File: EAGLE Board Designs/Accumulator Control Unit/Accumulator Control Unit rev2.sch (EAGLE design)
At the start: 210 parts, among them J1 CONNECTOR-CAN_MF_T_V_, J2 CONNECTOR-8_MF_T_V_, J3 CONNECTOR-8_MF_T_V_, J4 CONNECTOR-2_MF_T_V_, J5 CONNECTOR-12_MF_T_V_, J6 CONNECTOR-14_MF_T_V_, Q1 TRANSISTOR_N_MOS__PMV15ENEA, Q2 TRANSISTOR_N_MOS__PMV15ENEA, Q3 TRANSISTOR_N_MOS__PMV15ENEA, Q4 TRANSISTOR_N_MOS__PMV15ENEA, T1 TRANSFORMER_HM2112ZNLT_AIRGAP, U1 RELAY_SOLIDSTATE_NO, U10 OPAMP_1_CHANNEL_OPA991, U11 LOGICGATE_AND_DCK3, U12 OPAMP_1_CHANNEL_OPA991, U13 OPAMP_1_CHANNEL_OPA991, U14 OPAMP_1_CHANNEL_OPA991, U15 LOGICGATE_AND_DCK3, U16 RELAY_SOLIDSTATE_NO, U17 VOLTAGE_REGULATOR_SOT223_3.3V, U18 OPAMP_1_CHANNEL_OPA991, U19 MAX7404, U2 ADG1423, U20 OPAMP_1_CHANNEL_OPA991, U21 LOGICGATE_BUFFER, U22 OPAMP_1_CHANNEL_OPA991, U25 TCAN1051HQV-Q1, U26 MAX7404, U27 OPAMP_1_CHANNEL_OPA991, U28 MAX7404, U29 OPAMP_1_CHANNEL_OPA991, U3 LM555, U30 MAX7404, U4 OPAMP_1_CHANNEL_OPA991, U5 LTC6820, U6 ADM8316WBX30, U7 OPAMP_1_CHANNEL_OPA991, U8 LOGICGATE_AND_DCK3, U9 OPAMP_1_CHANNEL_OPA991

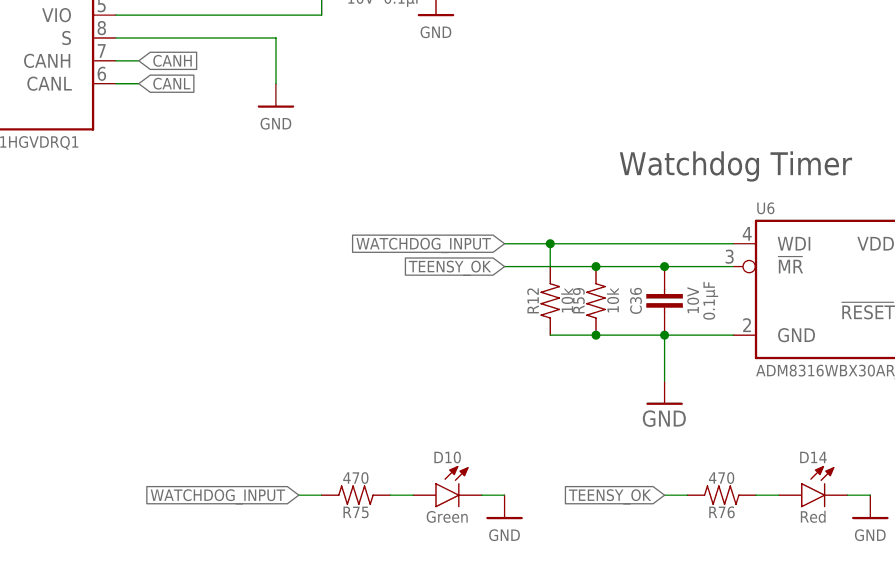
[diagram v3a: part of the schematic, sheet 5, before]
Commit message: all changes but board to board complete
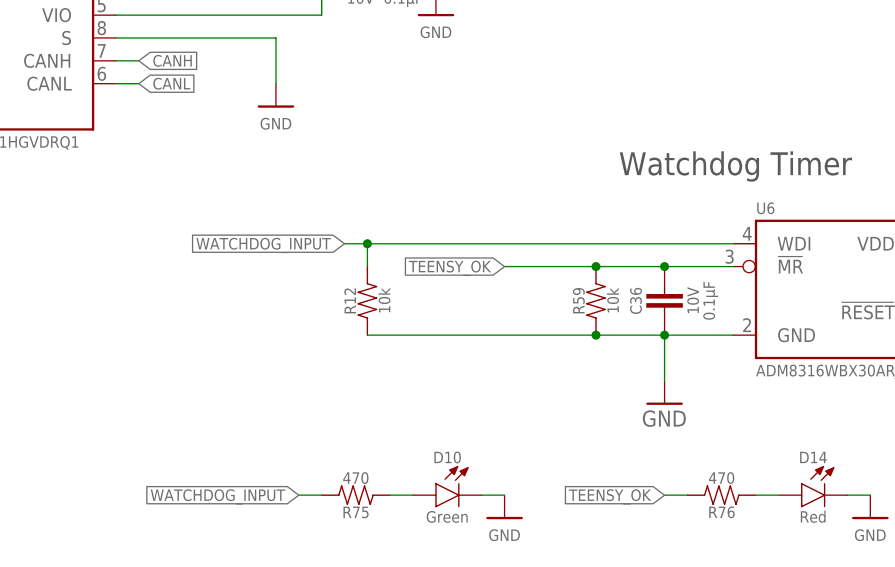
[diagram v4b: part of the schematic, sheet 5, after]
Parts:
- J1: value CONNECTOR-CAN_MF_T_V_ -> CONNECTOR-CAN_μF_S_RA_; device HyTechDevices - Copy:CONNECTOR-CAN_MF_T_V_ -> HyTechDevices:CONNECTOR-CAN_μF_S_RA_
- renumbered U$2 to U40
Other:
- moved on the sheet: R12
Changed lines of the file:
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@@
 <part name="D4" library="HyTechDevices - Copy" deviceset="TVS_*" device="" technology="8V"/>
 <part name="P5" library="HyTechSupplies" deviceset="GND" device=""/>
-<part name="J1" library="HyTechDevices - Copy" deviceset="CONNECTOR-CAN_?_*" device="MF_T_V"/>
+<part name="J1" library="HyTechDevices" deviceset="CONNECTOR-CAN_?_*" device="μF_S_RA"/>
 <part name="J5" library="HyTechDevices - Copy" deviceset="CONNECTOR-12_?_*" device="MF_T_V"/>
 <part name="J6" library="HyTechDevices - Copy" deviceset="CONNECTOR-14_?_*" device="MF_T_V"/>
@@
 <part name="R57" library="HyTechDevices" deviceset="RESISTOR_?_*" device="0603" technology="470"/>
 <part name="GND8" library="HyTechSupplies" deviceset="GND" device=""/>
-<part name="U$2" library="HyTechDevices" deviceset="RELAY_SOLIDSTATE_NO" device=""/>
+<part name="U40" library="HyTechDevices" deviceset="RELAY_SOLIDSTATE_NO" device=""/>
 <part name="R58" library="HyTechDevices - Copy" deviceset="RESISTOR_?_*" device="0603" technology="10K"/>
 <part name="R63" library="HyTechDevices - Copy" deviceset="RESISTOR_?_*" device="0603" technology="12K"/>
@@
 <attribute name="VALUE" x="228.6" y="168.91" size="1.27" layer="96" align="top-center"/>
 </instance>
-<instance part="P25" gate="1" x="38.1" y="99.06" smashed="yes">
-<attribute name="VALUE" x="38.1" y="97.79" size="1.27" layer="96" align="top-center"/>
+<instance part="P25" gate="1" x="38.1" y="101.6" smashed="yes">
+<attribute name="VALUE" x="38.1" y="100.33" size="1.27" layer="96" align="top-center"/>
 </instance>
 <instance part="U2" gate="S2" x="109.22" y="114.3" smashed="yes">
@@
 <pinref part="P25" gate="1" pin="GND"/>
 <wire x1="20.32" y1="104.14" x2="38.1" y2="104.14" width="0.1524" layer="91"/>
-<wire x1="38.1" y1="104.14" x2="38.1" y2="101.6" width="0.1524" layer="91"/>
 </segment>
 <segment>
@@
 </segment>
 <segment>
-<wire x1="22.86" y1="88.9" x2="25.4" y2="88.9" width="0.1524" layer="91"/>
+<pinref part="CURRENT_SENSE" gate="G$1" pin="P$1"/>
 <wire x1="22.86" y1="88.9" x2="25.4" y2="88.9" width="0.1524" layer="91"/>
 <label x="25.4" y="88.9" size="1.27" layer="95" xref="yes"/>
-<pinref part="CURRENT_SENSE" gate="G$1" pin="P$1"/>
 </segment>
 </net>
@@
 <attribute name="VALUE" x="203.2" y="115.57" size="1.27" layer="96" align="top-center"/>
 </instance>
-<instance part="U$2" gate="G$1" x="208.28" y="132.08" smashed="yes">
+<instance part="U40" gate="G$1" x="208.28" y="132.08" smashed="yes">
 <attribute name="NAME" x="208.28" y="132.842" size="1.27" layer="95"/>
 <attribute name="MPN" x="208.28" y="118.618" size="1.27" layer="96" align="top-left"/>
@@
 <wire x1="203.2" y1="121.92" x2="203.2" y2="119.38" width="0.1524" layer="91"/>
 <pinref part="GND8" gate="1" pin="GND"/>
-<pinref part="U$2" gate="G$1" pin="CONTROL-"/>
+<pinref part="U40" gate="G$1" pin="CONTROL-"/>
 </segment>
 <segment>
@@
 </segment>
 <segment>
-<pinref part="U$2" gate="G$1" pin="CONTACT2"/>
+<pinref part="U40" gate="G$1" pin="CONTACT2"/>
 <wire x1="228.6" y1="129.54" x2="231.14" y2="129.54" width="0.1524" layer="91"/>
 <wire x1="231.14" y1="129.54" x2="231.14" y2="134.62" width="0.1524" layer="91"/>
@@
 <wire x1="233.68" y1="116.84" x2="236.22" y2="116.84" width="0.1524" layer="91"/>
 <label x="236.22" y="116.84" size="1.27" layer="95" xref="yes"/>
-<pinref part="U$2" gate="G$1" pin="CONTACT1"/>
+<pinref part="U40" gate="G$1" pin="CONTACT1"/>
 <wire x1="228.6" y1="121.92" x2="233.68" y2="121.92" width="0.1524" layer="91"/>
 <junction x="233.68" y="121.92"/>
@@
 <pinref part="R57" gate="G$1" pin="2"/>
 <wire x1="200.66" y1="129.54" x2="205.74" y2="129.54" width="0.1524" layer="91"/>
-<pinref part="U$2" gate="G$1" pin="CONTROL+"/>
+<pinref part="U40" gate="G$1" pin="CONTROL+"/>
 </segment>
 </net>
@@
 <attribute name="VALUE" x="243.84" y="113.03" size="1.27" layer="96" align="bottom-center"/>
 </instance>
-<instance part="R12" gate="G$1" x="195.58" y="88.9" smashed="yes" rot="R90">
-<attribute name="NAME" x="194.31" y="87.63" size="1.27" layer="95" rot="R90" align="bottom-center"/>
-<attribute name="RESISTANCE" x="196.85" y="87.63" size="1.27" layer="96" rot="R90" align="top-center"/>
+<instance part="R12" gate="G$1" x="175.26" y="88.9" smashed="yes" rot="R90">
+<attribute name="NAME" x="173.99" y="87.63" size="1.27" layer="95" rot="R90" align="bottom-center"/>
+<attribute name="RESISTANCE" x="176.53" y="87.63" size="1.27" layer="96" rot="R90" align="top-center"/>
 </instance>
 <instance part="GND38" gate="1" x="208.28" y="76.2" smashed="yes">
@@
 <segment>
 <pinref part="R12" gate="G$1" pin="1"/>
-<wire x1="195.58" y1="83.82" x2="200.66" y2="83.82" width="0.1524" layer="91"/>
+<wire x1="175.26" y1="83.82" x2="200.66" y2="83.82" width="0.1524" layer="91"/>
 <pinref part="R59" gate="G$1" pin="1"/>
 <wire x1="200.66" y1="83.82" x2="208.28" y2="83.82" width="0.1524" layer="91"/>
@@
 <segment>
 <pinref part="R12" gate="G$1" pin="2"/>
-<wire x1="195.58" y1="93.98" x2="215.9" y2="93.98" width="0.1524" layer="91"/>
-<wire x1="195.58" y1="93.98" x2="195.58" y2="91.44" width="0.1524" layer="91"/>
-<label x="190.5" y="93.98" size="1.27" layer="95" rot="R180" xref="yes"/>
-<wire x1="195.58" y1="93.98" x2="190.5" y2="93.98" width="0.1524" layer="91"/>
-<junction x="195.58" y="93.98"/>
+<wire x1="175.26" y1="93.98" x2="215.9" y2="93.98" width="0.1524" layer="91"/>
+<wire x1="175.26" y1="93.98" x2="175.26" y2="91.44" width="0.1524" layer="91"/>
+<label x="172.72" y="93.98" size="1.27" layer="95" rot="R180" xref="yes"/>
+<wire x1="175.26" y1="93.98" x2="172.72" y2="93.98" width="0.1524" layer="91"/>
+<junction x="175.26" y="93.98"/>
 <pinref part="U6" gate="G$1" pin="WDI"/>
 </segment>

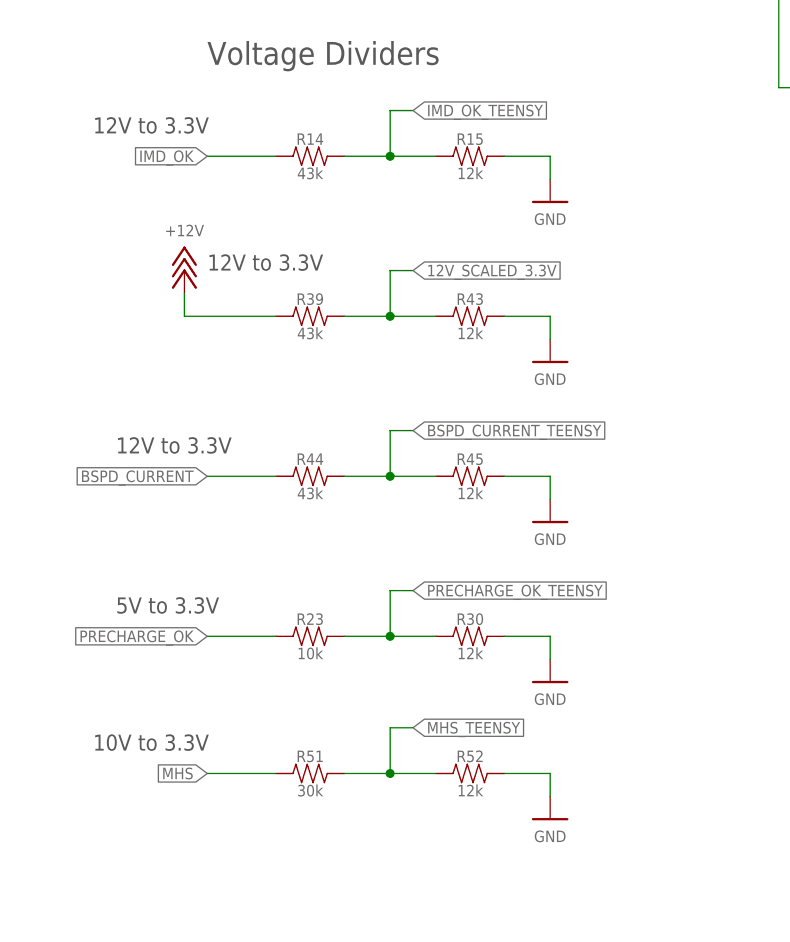
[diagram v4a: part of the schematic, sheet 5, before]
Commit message: changed voltage dividers
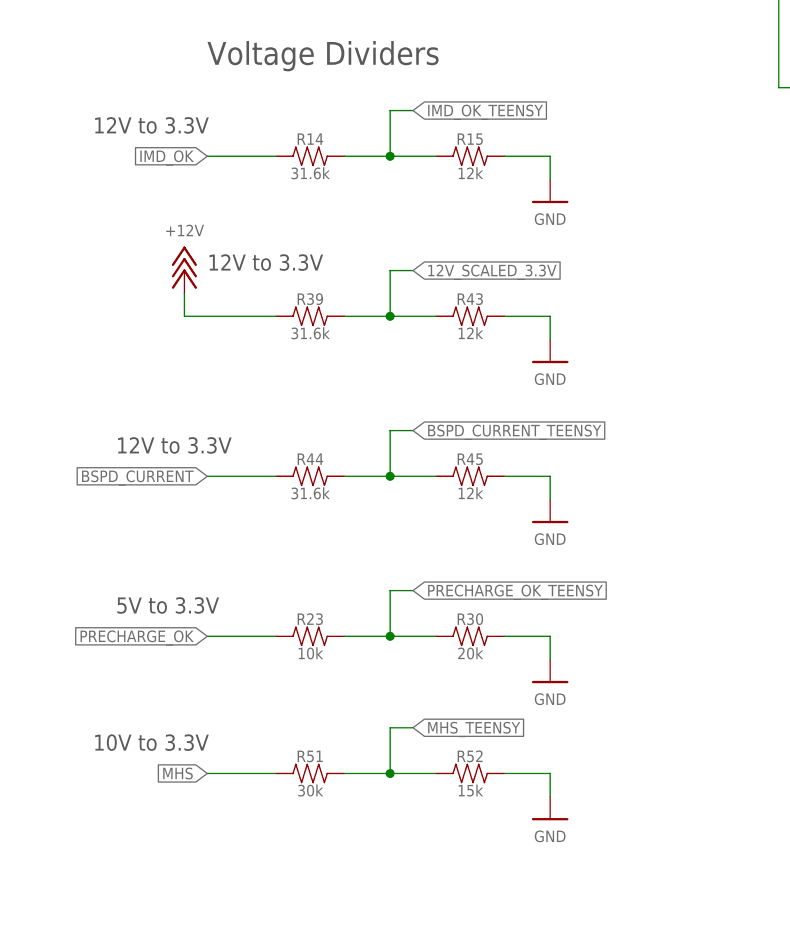
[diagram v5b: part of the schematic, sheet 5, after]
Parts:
- R14, R39, R44: value RESISTOR_0603_43K -> RESISTOR_0603_31.6K; device HyTechDevices - Copy:RESISTOR_0603_43K -> HyTechDevices:RESISTOR_0603_31.6K
- R30: value RESISTOR_0603_12K -> RESISTOR_0603_20K; device HyTechDevices - Copy:RESISTOR_0603_12K -> HyTechDevices:RESISTOR_0603_20K
- R52: value RESISTOR_0603_12K -> RESISTOR_0603_15K; device HyTechDevices - Copy:RESISTOR_0603_12K -> HyTechDevices:RESISTOR_0603_15K
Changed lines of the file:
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@@
 <part name="P58" library="HyTechSupplies" deviceset="GND" device=""/>
 <part name="P59" library="HyTechSupplies" deviceset="GND" device=""/>
-<part name="R14" library="HyTechDevices - Copy" deviceset="RESISTOR_?_*" device="0603" technology="43K"/>
+<part name="R14" library="HyTechDevices" deviceset="RESISTOR_?_*" device="0603" technology="31.6K" value="RESISTOR_0603_31.6K"/>
 <part name="R15" library="HyTechDevices - Copy" deviceset="RESISTOR_?_*" device="0603" technology="12K"/>
 <part name="P66" library="HyTechSupplies" deviceset="GND" device=""/>
 <part name="P67" library="HyTechSupplies" deviceset="GND" device=""/>
-<part name="R39" library="HyTechDevices - Copy" deviceset="RESISTOR_?_*" device="0603" technology="43K"/>
+<part name="R39" library="HyTechDevices" deviceset="RESISTOR_?_*" device="0603" technology="31.6K" value="RESISTOR_0603_31.6K"/>
 <part name="P68" library="HyTechSupplies" deviceset="GND" device=""/>
-<part name="R44" library="HyTechDevices - Copy" deviceset="RESISTOR_?_*" device="0603" technology="43K"/>
+<part name="R44" library="HyTechDevices" deviceset="RESISTOR_?_*" device="0603" technology="31.6K" value="RESISTOR_0603_31.6K"/>
 <part name="P69" library="HyTechSupplies" deviceset="GND" device=""/>
 <part name="P70" library="HyTechSupplies" deviceset="+12V" device=""/>
-<part name="R30" library="HyTechDevices - Copy" deviceset="RESISTOR_?_*" device="0603" technology="12K"/>
+<part name="R30" library="HyTechDevices" deviceset="RESISTOR_?_*" device="0603" technology="20K" value="RESISTOR_0603_20K"/>
 <part name="R23" library="HyTechDevices - Copy" deviceset="RESISTOR_?_*" device="0603" technology="10K"/>
 <part name="P72" library="HyTechSupplies" deviceset="+3V3" device=""/>
@@
 <part name="P82" library="HyTechSupplies" deviceset="GND" device=""/>
 <part name="C43" library="HyTechDevices - Copy" deviceset="CAPACITOR_?_*" device="0603" technology="10V_680PF"/>
-<part name="R52" library="HyTechDevices - Copy" deviceset="RESISTOR_?_*" device="0603" technology="12K"/>
+<part name="R52" library="HyTechDevices" deviceset="RESISTOR_?_*" device="0603" technology="15K" value="RESISTOR_0603_15K"/>
 <part name="P87" library="HyTechSupplies" deviceset="GND" device=""/>
 <part name="R51" library="HyTechDevices - Copy" deviceset="RESISTOR_?_*" device="0603" technology="30K"/>

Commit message: more changes
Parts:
- J3: value CONNECTOR-8_MF_T_V_ -> CONNECTOR-8_FS_S; device HyTechDevices - Copy:CONNECTOR-8_MF_T_V_ -> HyTechDevices:CONNECTOR-8_FS_S
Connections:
- net +12V: now also J3.5; no longer J3.1
- net GND: now also J3.8; no longer J3.4
- net ISO_PACK+: now also J3.1; no longer J3.5
- net ISO_PACK-: now also J3.2; no longer J3.6
- net ISO_TS+: now also J3.3; no longer J3.7
- net ISO_TS-: now also J3.4; no longer J3.8
- net PRECHARGE_OK: now also J3.7; no longer J3.3
- net SHDN: now also J3.6; no longer J3.2
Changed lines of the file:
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@@
 <part name="FRAME2" library="HyTechFrames" deviceset="FRAME" device=""/>
 <part name="FRAME4" library="HyTechFrames" deviceset="FRAME" device=""/>
-<part name="J3" library="HyTechDevices - Copy" deviceset="CONNECTOR-8_?_*" device="MF_T_V"/>
+<part name="J3" library="HyTechDevices" deviceset="CONNECTOR-8_?_*" device="FS" technology="S"/>
 <part name="P1" library="HyTechSupplies" deviceset="+12V" device=""/>
 <part name="P2" library="HyTechSupplies" deviceset="GND" device=""/>
@@
 <attribute name="VALUE" x="27.94" y="179.07" size="1.27" layer="96" align="top-center"/>
 </instance>
-<instance part="P6" gate="1" x="40.64" y="170.18" smashed="yes">
-<attribute name="VALUE" x="40.64" y="173.99" size="1.27" layer="96" align="bottom-center"/>
+<instance part="P6" gate="1" x="50.8" y="160.02" smashed="yes">
+<attribute name="VALUE" x="50.8" y="163.83" size="1.27" layer="96" align="bottom-center"/>
 </instance>
 <instance part="P11" gate="1" x="88.9" y="177.8" smashed="yes">
@@
 <attribute name="RESISTANCE" x="255.27" y="113.03" size="1.27" layer="96" rot="R180" align="top-center"/>
 </instance>
-<instance part="P5" gate="1" x="43.18" y="152.4" smashed="yes">
-<attribute name="VALUE" x="43.18" y="151.13" size="1.27" layer="96" align="top-center"/>
+<instance part="P5" gate="1" x="22.86" y="144.78" smashed="yes">
+<attribute name="VALUE" x="22.86" y="143.51" size="1.27" layer="96" align="top-center"/>
 </instance>
 <instance part="J1" gate="G$1" x="10.16" y="195.58" smashed="yes">
@@
 <net name="SHDN" class="0">
 <segment>
-<pinref part="J3" gate="G$1" pin="2"/>
-<wire x1="20.32" y1="162.56" x2="22.86" y2="162.56" width="0.1524" layer="91"/>
-<label x="22.86" y="162.56" size="1.27" layer="95" xref="yes"/>
+<wire x1="20.32" y1="152.4" x2="22.86" y2="152.4" width="0.1524" layer="91"/>
+<label x="22.86" y="152.4" size="1.27" layer="95" xref="yes"/>
+<pinref part="J3" gate="G$1" pin="6"/>
 </segment>
 <segment>
@@
 <net name="ISO_PACK+" class="0">
 <segment>
-<pinref part="J3" gate="G$1" pin="5"/>
-<wire x1="20.32" y1="154.94" x2="22.86" y2="154.94" width="0.1524" layer="91"/>
-<label x="22.86" y="154.94" size="1.27" layer="95" xref="yes"/>
+<wire x1="20.32" y1="165.1" x2="22.86" y2="165.1" width="0.1524" layer="91"/>
+<label x="22.86" y="165.1" size="1.27" layer="95" xref="yes"/>
+<pinref part="J3" gate="G$1" pin="1"/>
 </segment>
 </net>
 <net name="ISO_PACK-" class="0">
 <segment>
-<pinref part="J3" gate="G$1" pin="6"/>
-<wire x1="20.32" y1="152.4" x2="22.86" y2="152.4" width="0.1524" layer="91"/>
-<label x="22.86" y="152.4" size="1.27" layer="95" xref="yes"/>
+<wire x1="20.32" y1="162.56" x2="22.86" y2="162.56" width="0.1524" layer="91"/>
+<label x="22.86" y="162.56" size="1.27" layer="95" xref="yes"/>
+<pinref part="J3" gate="G$1" pin="2"/>
 </segment>
 </net>
 <net name="ISO_TS+" class="0">
 <segment>
-<pinref part="J3" gate="G$1" pin="7"/>
-<wire x1="20.32" y1="149.86" x2="22.86" y2="149.86" width="0.1524" layer="91"/>
-<label x="22.86" y="149.86" size="1.27" layer="95" xref="yes"/>
+<wire x1="20.32" y1="160.02" x2="22.86" y2="160.02" width="0.1524" layer="91"/>
+<label x="22.86" y="160.02" size="1.27" layer="95" xref="yes"/>
+<pinref part="J3" gate="G$1" pin="3"/>
 </segment>
 </net>
 <net name="ISO_TS-" class="0">
 <segment>
-<pinref part="J3" gate="G$1" pin="8"/>
-<wire x1="20.32" y1="147.32" x2="22.86" y2="147.32" width="0.1524" layer="91"/>
-<label x="22.86" y="147.32" size="1.27" layer="95" xref="yes"/>
+<wire x1="20.32" y1="157.48" x2="22.86" y2="157.48" width="0.1524" layer="91"/>
+<label x="22.86" y="157.48" size="1.27" layer="95" xref="yes"/>
+<pinref part="J3" gate="G$1" pin="4"/>
 </segment>
 </net>
@@
 <pinref part="P31" gate="1" pin="GND"/>
 <pinref part="R60" gate="G$1" pin="1"/>
-</segment>
-<segment>
-<pinref part="J3" gate="G$1" pin="4"/>
-<pinref part="P5" gate="1" pin="GND"/>
-<wire x1="20.32" y1="157.48" x2="43.18" y2="157.48" width="0.1524" layer="91"/>
-<wire x1="43.18" y1="157.48" x2="43.18" y2="154.94" width="0.1524" layer="91"/>
 </segment>
 <segment>
@@
 <pinref part="D15" gate="G$1" pin="A"/>
 </segment>
+<segment>
+<pinref part="P5" gate="1" pin="GND"/>
+<wire x1="22.86" y1="147.32" x2="20.32" y2="147.32" width="0.1524" layer="91"/>
+<pinref part="J3" gate="G$1" pin="8"/>
+</segment>
 </net>
 <net name="+12V" class="0">
@@
 </segment>
 <segment>
-<wire x1="40.64" y1="165.1" x2="40.64" y2="167.64" width="0.1524" layer="91"/>
+<wire x1="50.8" y1="154.94" x2="50.8" y2="157.48" width="0.1524" layer="91"/>
 <pinref part="P6" gate="1" pin="+12V"/>
-<pinref part="J3" gate="G$1" pin="1"/>
-<wire x1="20.32" y1="165.1" x2="40.64" y2="165.1" width="0.1524" layer="91"/>
+<pinref part="J3" gate="G$1" pin="5"/>
+<wire x1="20.32" y1="154.94" x2="50.8" y2="154.94" width="0.1524" layer="91"/>
 </segment>
 <segment>
@@
 <net name="PRECHARGE_OK" class="0">
 <segment>
-<wire x1="20.32" y1="160.02" x2="22.86" y2="160.02" width="0.1524" layer="91"/>
-<label x="22.86" y="160.02" size="1.27" layer="95" xref="yes"/>
-<pinref part="J3" gate="G$1" pin="3"/>
-</segment>
-</net>
+<wire x1="20.32" y1="149.86" x2="22.86" y2="149.86" width="0.1524" layer="91"/>
+<label x="22.86" y="149.86" size="1.27" layer="95" xref="yes"/>
+<pinref part="J3" gate="G$1" pin="7"/>
+</segment>
+</net>

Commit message: tvs diodes
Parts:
- added D12, D5, D7, D8, D9: TVS_15V, HyTechDevices:TVS_15V
- R14, R39, R44: value RESISTOR_0603_31.6K -> RESISTOR_0603_33K; device HyTechDevices:RESISTOR_0603_31.6K -> HyTechDevices:RESISTOR_0603_33K
- R23: value RESISTOR_0603_10K -> RESISTOR_0603_18.7K; device HyTechDevices - Copy:RESISTOR_0603_10K -> HyTechDevices:RESISTOR_0603_18.7K
- R30: value RESISTOR_0603_20K -> RESISTOR_0603_33K; device HyTechDevices:RESISTOR_0603_20K -> HyTechDevices:RESISTOR_0603_33K
- R51: value RESISTOR_0603_30K -> RESISTOR_0603_33K; device HyTechDevices - Copy:RESISTOR_0603_30K -> HyTechDevices:RESISTOR_0603_33K
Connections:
- net +12V: now also D9.C
- net BSPD_CURRENT: now also D8.C
- net GND: now also D12.A, D5.A, D7.A, D8.A, D9.A
- net IMD_OK: now also D12.C
- net MHS: now also D5.C
- net PRECHARGE_OK: now also D7.C
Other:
- moved on the sheet: R51, R52
